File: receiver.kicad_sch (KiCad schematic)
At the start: 0 parts

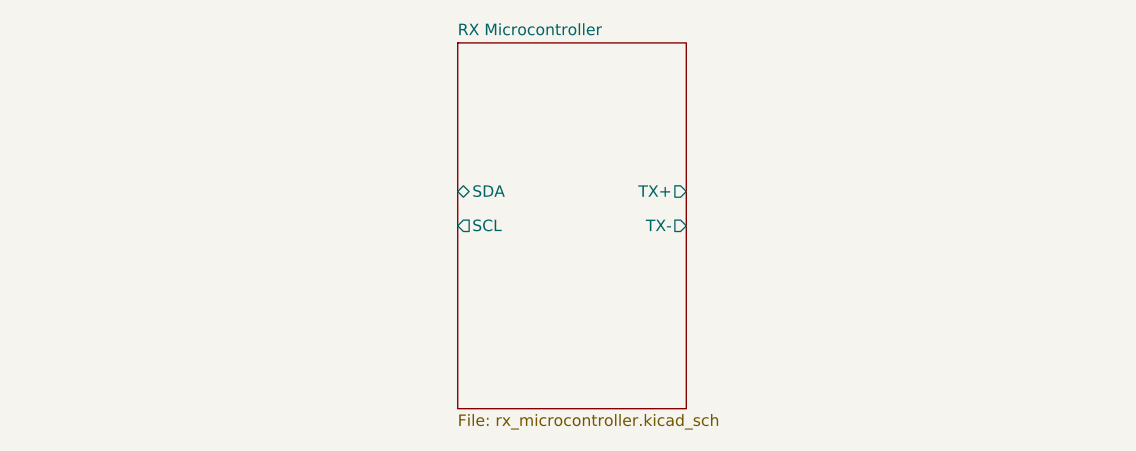
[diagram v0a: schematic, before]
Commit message: Finished schematic, added power section for external power (both power supply and battery), added current sensing for TX microcontroller
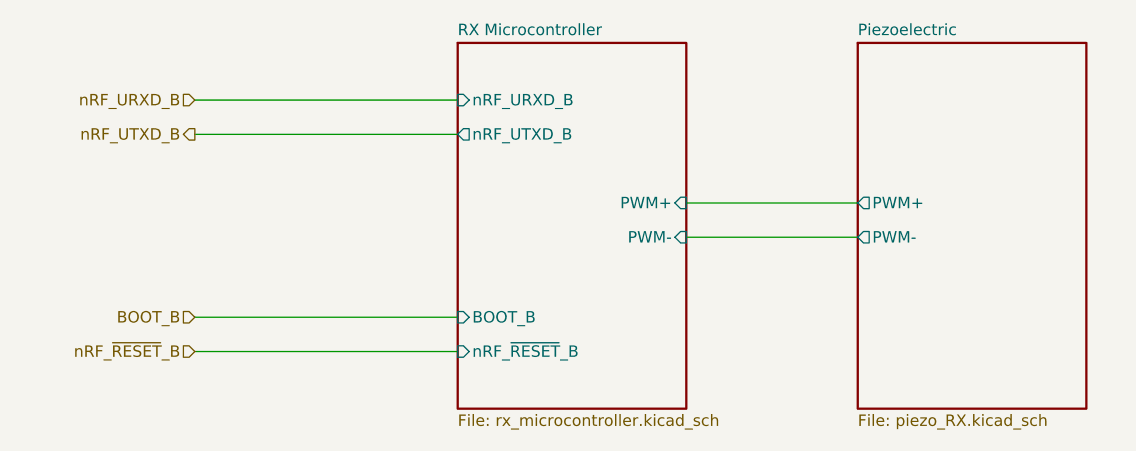
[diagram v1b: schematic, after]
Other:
- added sheet Piezoelectric (piezo_RX.kicad_sch)
- sheet RX Microcontroller ports: added BOOT_B, PWM+, PWM-, nRF_URXD_B, nRF_UTXD_B, nRF_~{RESET}_B; removed SCL, SDA, TX+, TX-
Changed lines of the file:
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@@
 		(company "UVM SEED Team 512 - NWTL")
+	)
+	(wire
+		(pts
+			(xy 101.6 83.82) (xy 130.81 83.82)
+		)
+		(stroke
+			(width 0)
+			(type default)
+		)
+	)
+	(wire
+		(pts
+			(xy 156.21 99.06) (xy 175.26 99.06)
+		)
+		(stroke
+			(width 0)
+			(type default)
+		)
+	)
+	(wire
+		(pts
+			(xy 101.6 107.95) (xy 130.81 107.95)
+		)
+		(stroke
+			(width 0)
+			(type default)
+		)
+	)
+	(wire
+		(pts
+			(xy 101.6 111.76) (xy 130.81 111.76)
+		)
+		(stroke
+			(width 0)
+			(type default)
+		)
+	)
+	(wire
+		(pts
+			(xy 156.21 95.25) (xy 175.26 95.25)
+		)
+		(stroke
+			(width 0)
+			(type default)
+		)
+	)
+	(wire
+		(pts
+			(xy 101.6 87.63) (xy 130.81 87.63)
+		)
+		(stroke
+			(width 0)
+			(type default)
+		)
+	)
+	(hierarchical_label "BOOT_B"
+		(shape input)
+		(at 101.6 107.95 180)
+		(effects
+			(font
+				(size 1.27 1.27)
+			)
+			(justify right)
+		)
+	)
+	(hierarchical_label "nRF_~{RESET}_B"
+		(shape input)
+		(at 101.6 111.76 180)
+		(effects
+			(font
+				(size 1.27 1.27)
+			)
+			(justify right)
+		)
+	)
+	(hierarchical_label "nRF_URXD_B"
+		(shape input)
+		(at 101.6 83.82 180)
+		(effects
+			(font
+				(size 1.27 1.27)
+			)
+			(justify right)
+		)
+	)
+	(hierarchical_label "nRF_UTXD_B"
+		(shape output)
+		(at 101.6 87.63 180)
+		(effects
+			(font
+				(size 1.27 1.27)
+			)
+			(justify right)
+		)
 	)
 	(sheet
@@
 		(fields_autoplaced yes)
 		(stroke
-			(width 0.1524)
+			(width 0.254)
 			(type solid)
 		)
 		(fill
-			(color 0 0 0 0)
+			(color 255 255 194 1)
 		)
 		(property "Sheetname" "RX Microcontroller"
@@
 			)
 		)
-		(pin "TX-" output
-			(at 156.21 97.79 0)
+		(pin "nRF_URXD_B" input
+			(at 130.81 83.82 180)
+			(effects
+				(font
+					(size 1.27 1.27)
+				)
+				(justify left)
+			)
+		)
+		(pin "nRF_~{RESET}_B" input
+			(at 130.81 111.76 180)
+			(effects
+				(font
+					(size 1.27 1.27)
+				)
+				(justify left)
+			)
+		)
+		(pin "BOOT_B" input
+			(at 130.81 107.95 180)
+			(effects
+				(font
+					(size 1.27 1.27)
+				)
+				(justify left)
+			)
+		)
+		(pin "PWM-" input
+			(at 156.21 99.06 0)
 			(effects
 				(font
@@
 			)
 		)
-		(pin "TX+" output
-			(at 156.21 93.98 0)
+		(pin "PWM+" input
+			(at 156.21 95.25 0)
 			(effects
 				(font
@@
 			)
 		)
-		(pin "SCL" output
-			(at 130.81 97.79 180)
-			(effects
-				(font
-					(size 1.27 1.27)
-				)
-				(justify left)
-			)
-		)
-		(pin "SDA" bidirectional
-			(at 130.81 93.98 180)
+		(pin "nRF_UTXD_B" output
+			(at 130.81 87.63 180)
 			(effects
 				(font
@@
 				)
 			)
+		)
+	)
+	(sheet
+		(at 175.26 77.47)
+		(size 25.4 40.64)
+		(exclude_from_sim no)
+		(in_bom yes)
+		(on_board yes)
+		(dnp no)
+		(fields_autoplaced yes)
+		(stroke
+			(width 0.254)
+			(type solid)
+		)
+		(fill
+			(color 255 255 194 1)
+		)
+		(property "Sheetname" "Piezoelectric"
+			(at 175.26 76.7584 0)
+			(show_name no)
+			(do_not_autoplace no)
+			(effects
+				(font
+					(size 1.27 1.27)
+				)
+				(justify left bottom)
+			)
+		)
+		(property "Sheetfile" "piezo_RX.kicad_sch"
+			(at 175.26 118.6946 0)
+			(show_name no)
+			(do_not_autoplace no)
+			(effects
+				(font
+					(size 1.27 1.27)
+				)
+				(justify left top)
+			)
+		)
+		(pin "PWM+" output
+			(at 175.26 95.25 180)
+			(effects
+				(font
+					(size 1.27 1.27)
+				)
+				(justify left)
+			)
+		)
+		(pin "PWM-" output
+			(at 175.26 99.06 180)
+			(effects
+				(font
+					(size 1.27 1.27)
+				)
+				(justify left)
+			)
+		)
+		(instances
+			(project "Temp-Logger"
+				(path "/9c5f4d5b-9930-4cae-a7d7-03685cadac72/8722ad6e-d449-40f5-b9d3-e719432ce7be"
+					(page "11")
+				)
+			)
